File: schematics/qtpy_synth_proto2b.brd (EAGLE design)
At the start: 76.2 x 63.5 mm, 25 parts, among them IC1 H11L1MS, J1 AUDIO-JACK-TRRS, J2 AUDIO-JACK-TRRS, P1 10k, P2 10k, U1 ADAFRUIT_QTPYM0

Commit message: sync up
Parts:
- DISP: value DISPLAY-OLED-128X64-I2C -> DISPLAY-OLED-128X64-I2CTOD; device diy-modules:DISPLAY-OLED-128X64-I2C -> todstuff2023:DISPLAY-OLED-128X64-I2C-TOD
- moved SW 2.54 mm to (38.1, 15.2)
- moved P1 2.54 mm to (14.0, 25.4)
- moved P2 2.54 mm to (62.2, 25.4)
- moved U1 0.76 mm to (14.5, 47.0)
- renumbered C11 to C1
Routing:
- net +3V3: track 154.1 -> 150.7 mm
- net POTA: track 43.9 -> 41.7 mm
- net POTB: track 75.0 -> 73.1 mm
- net TP4: track 75.1 -> 74.3 mm
- net TP2: track 74.5 -> 75.3 mm
- net SDA: track 50.8 -> 50.1 mm
- net PWM_AUDIO: track 40.0 -> 40.8 mm
- net MIDI_IN: track 37.5 -> 38.3 mm
- net SCL: track 47.8 -> 47.0 mm
- net SW: track 67.0 -> 67.7 mm
- net TP3: track 68.5 -> 69.2 mm
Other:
- board text added: "Parts: - QTPy RP2040 - 0.9" I2C OLED SSD1306 - 2x 10k pots - tact switch - 2x PJ320D 3.5mm jacks - IC1: H11L1 optoisolator - D1: 1N4148 - R1-4: 1M, R5: 4.7k, R6,R7: 220, R8:100: R9 1.8k - C1,C2: 100nF, C3: 47uF"
- board text added: "qtpy_synth_proto2b"
- board text removed: "Parts: - QTPy RP2040 - 0.9" I2C OLED SSD1306 - 2x 10k pots - tact switch - IC1: H11L1 optoisolator - D1: 1N4148 - R1-4: 1M, R5: 4.7k, R6,R7: 220, R8:100: R9 1.8k - C1,C2: 100nF, C3: 47uF"
- board text removed: "qtpy_synth_proto2a"

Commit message: more progress on synthio_instrument
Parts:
- moved P1 2.54 mm to (14.0, 22.9)
- moved P2 2.54 mm to (62.2, 22.9)
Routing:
- net SW: track 67.7 -> 70.9 mm
- net POTB: track 73.1 -> 75.8 mm
- net POTA: track 41.7 -> 44.2 mm
- net TP1: track 53.1 -> 55.4 mm
- net TP2: track 75.3 -> 77.1 mm
- net +3V3: track 150.7 -> 151.3 mm

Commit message: gerbers for proto2b
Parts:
- moved R4 2.74 mm to (62.2, 11.4)
- moved R1 0.76 mm to (14.0, 11.4)
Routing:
- net TP4: track 74.3 -> 76.4 mm
- net TP1: track 55.4 -> 56.6 mm
- net TP2: track 77.1 -> 76.1 mm
- net MIDI_IN: track 38.3 -> 37.4 mm
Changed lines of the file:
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@@
 <layer number="14" name="Route14" color="1" fill="6" visible="no" active="no"/>
 <layer number="15" name="Route15" color="4" fill="6" visible="no" active="no"/>
-<layer number="16" name="Bottom" color="1" fill="1" visible="yes" active="yes"/>
+<layer number="16" name="Bottom" color="1" fill="1" visible="no" active="yes"/>
 <layer number="17" name="Pads" color="2" fill="1" visible="yes" active="yes"/>
 <layer number="18" name="Vias" color="2" fill="1" visible="yes" active="yes"/>
@@
 <layer number="20" name="Dimension" color="15" fill="1" visible="yes" active="yes"/>
 <layer number="21" name="tPlace" color="14" fill="1" visible="yes" active="yes"/>
-<layer number="22" name="bPlace" color="13" fill="1" visible="yes" active="yes"/>
+<layer number="22" name="bPlace" color="13" fill="1" visible="no" active="yes"/>
 <layer number="23" name="tOrigins" color="15" fill="1" visible="yes" active="yes"/>
-<layer number="24" name="bOrigins" color="15" fill="1" visible="yes" active="yes"/>
+<layer number="24" name="bOrigins" color="15" fill="1" visible="no" active="yes"/>
 <layer number="25" name="tNames" color="7" fill="1" visible="yes" active="yes"/>
-<layer number="26" name="bNames" color="7" fill="1" visible="yes" active="yes"/>
+<layer number="26" name="bNames" color="7" fill="1" visible="no" active="yes"/>
 <layer number="27" name="tValues" color="7" fill="1" visible="no" active="yes"/>
 <layer number="28" name="bValues" color="7" fill="1" visible="no" active="yes"/>
@@
 <layer number="38" name="bTest" color="7" fill="1" visible="no" active="yes"/>
 <layer number="39" name="tKeepout" color="4" fill="11" visible="yes" active="yes"/>
-<layer number="40" name="bKeepout" color="1" fill="11" visible="yes" active="yes"/>
+<layer number="40" name="bKeepout" color="1" fill="11" visible="no" active="yes"/>
 <layer number="41" name="tRestrict" color="4" fill="10" visible="yes" active="yes"/>
-<layer number="42" name="bRestrict" color="1" fill="10" visible="yes" active="yes"/>
+<layer number="42" name="bRestrict" color="1" fill="10" visible="no" active="yes"/>
 <layer number="43" name="vRestrict" color="2" fill="10" visible="no" active="yes"/>
 <layer number="44" name="Drills" color="7" fill="1" visible="no" active="yes"/>
@@
 <layer number="50" name="dxf" color="7" fill="1" visible="no" active="yes"/>
 <layer number="51" name="tDocu" color="7" fill="1" visible="yes" active="yes"/>
-<layer number="52" name="bDocu" color="7" fill="1" visible="yes" active="yes"/>
+<layer number="52" name="bDocu" color="7" fill="1" visible="no" active="yes"/>
 <layer number="53" name="tGND_GNDA" color="7" fill="9" visible="no" active="no"/>
 <layer number="54" name="bGND_GNDA" color="1" fill="9" visible="no" active="no"/>
@@
 <text x="72.39" y="34.29" size="1.016" layer="22" ratio="10" rot="MR0">works with CircuitPython!</text>
 <wire x1="-2.54" y1="22.86" x2="77.47" y2="22.86" width="0.1524" layer="51" style="shortdash"/>
+<wire x1="-3.81" y1="11.43" x2="76.2" y2="11.43" width="0.1524" layer="51" style="shortdash"/>
 </plain>
 <attributes>
@@
 <attribute name="MPN" value="PJ-320D" x="63.5" y="58.42" size="1.778" layer="27" rot="R270" display="off"/>
 </element>
-<element name="R1" library="rcl" library_urn="urn:adsk.eagle:library:334" package="R0805" package3d_urn="urn:adsk.eagle:package:23553/2" value="1M" x="13.97" y="10.668" smashed="yes">
-<attribute name="NAME" x="13.589" y="11.684" size="1.016" layer="25" ratio="10"/>
-<attribute name="POPULARITY" value="86" x="13.97" y="10.668" size="1.778" layer="27" display="off"/>
-<attribute name="SPICEPREFIX" value="R" x="13.97" y="10.668" size="1.778" layer="27" display="off"/>
-<attribute name="VALUE" x="13.335" y="8.128" size="1.27" layer="27"/>
+<element name="R1" library="rcl" library_urn="urn:adsk.eagle:library:334" package="R0805" package3d_urn="urn:adsk.eagle:package:23553/2" value="1M" x="13.97" y="11.43" smashed="yes">
+<attribute name="NAME" x="13.589" y="12.446" size="1.016" layer="25" ratio="10"/>
+<attribute name="POPULARITY" value="86" x="13.97" y="11.43" size="1.778" layer="27" display="off"/>
+<attribute name="SPICEPREFIX" value="R" x="13.97" y="11.43" size="1.778" layer="27" display="off"/>
+<attribute name="VALUE" x="13.335" y="8.89" size="1.27" layer="27"/>
 </element>
 <element name="R2" library="rcl" library_urn="urn:adsk.eagle:library:334" package="R0805" package3d_urn="urn:adsk.eagle:package:23553/2" value="1M" x="29.21" y="15.24" smashed="yes">
@@
 <attribute name="VALUE" x="46.355" y="12.7" size="1.27" layer="27"/>
 </element>
-<element name="R4" library="rcl" library_urn="urn:adsk.eagle:library:334" package="R0805" package3d_urn="urn:adsk.eagle:package:23553/2" value="1M" x="59.69" y="10.414" smashed="yes">
-<attribute name="NAME" x="59.055" y="11.684" size="1.016" layer="25" ratio="10"/>
-<attribute name="POPULARITY" value="86" x="59.69" y="10.414" size="1.778" layer="27" display="off"/>
-<attribute name="SPICEPREFIX" value="R" x="59.69" y="10.414" size="1.778" layer="27" display="off"/>
-<attribute name="VALUE" x="59.055" y="7.874" size="1.27" layer="27"/>
+<element name="R4" library="rcl" library_urn="urn:adsk.eagle:library:334" package="R0805" package3d_urn="urn:adsk.eagle:package:23553/2" value="1M" x="62.23" y="11.43" smashed="yes">
+<attribute name="NAME" x="61.595" y="12.7" size="1.016" layer="25" ratio="10"/>
+<attribute name="POPULARITY" value="86" x="62.23" y="11.43" size="1.778" layer="27" display="off"/>
+<attribute name="SPICEPREFIX" value="R" x="62.23" y="11.43" size="1.778" layer="27" display="off"/>
+<attribute name="VALUE" x="61.595" y="8.89" size="1.27" layer="27"/>
 </element>
 <element name="DISP" library="todstuff2023" package="DISPLAY-OLED-128X64-I2C-TOD" value="DISPLAY-OLED-128X64-I2CTOD" x="38.1" y="35.56" smashed="yes" rot="R180">
@@
 <wire x1="45.974" y1="29.21" x2="44.45" y2="29.21" width="0.3048" layer="1"/>
 <wire x1="41.221" y1="29.21" x2="36.395" y2="34.036" width="0.254" layer="1"/>
-<wire x1="51.635" y1="33.02" x2="46.99" y2="33.02" width="0.254" layer="1"/>
-<wire x1="46.99" y1="33.02" x2="45.974" y2="32.004" width="0.254" layer="1"/>
-<wire x1="45.974" y1="32.004" x2="45.974" y2="29.21" width="0.254" layer="1"/>
+<wire x1="51.635" y1="33.02" x2="48.514" y2="33.02" width="0.254" layer="1"/>
+<wire x1="48.514" y1="33.02" x2="45.974" y2="30.48" width="0.254" layer="1"/>
+<wire x1="45.974" y1="30.48" x2="45.974" y2="29.21" width="0.254" layer="1"/>
 <wire x1="45.974" y1="29.21" x2="45.974" y2="27.94" width="0.254" layer="1"/>
 <wire x1="44.45" y1="29.21" x2="41.221" y2="29.21" width="0.254" layer="1"/>
@@
 <contactref element="U1" pad="A3"/>
 <wire x1="11.43" y1="2.54" x2="13.02" y2="4.13" width="0.3048" layer="1"/>
-<wire x1="13.02" y1="4.13" x2="13.02" y2="10.668" width="0.3048" layer="1"/>
+<wire x1="13.02" y1="4.13" x2="13.02" y2="11.43" width="0.3048" layer="1"/>
 <wire x1="9.398" y1="45.212" x2="9.398" y2="35.56" width="0.3048" layer="1"/>
-<wire x1="9.398" y1="35.56" x2="4.826" y2="30.988" width="0.3048" layer="1"/>
-<wire x1="4.826" y1="30.988" x2="4.826" y2="12.954" width="0.3048" layer="1"/>
-<wire x1="4.826" y1="12.954" x2="7.112" y2="10.668" width="0.3048" layer="1"/>
-<wire x1="7.112" y1="10.668" x2="13.02" y2="10.668" width="0.3048" layer="1"/>
+<wire x1="9.398" y1="35.56" x2="3.81" y2="29.972" width="0.3048" layer="1"/>
+<wire x1="3.81" y1="29.972" x2="3.81" y2="13.97" width="0.3048" layer="1"/>
+<wire x1="3.81" y1="13.97" x2="6.35" y2="11.43" width="0.3048" layer="1"/>
+<wire x1="6.35" y1="11.43" x2="13.02" y2="11.43" width="0.3048" layer="1"/>
 </signal>
 <signal name="TP2">
@@
 <wire x1="6.858" y1="49.53" x2="7.874" y2="49.53" width="0.3048" layer="1"/>
 <wire x1="11.176" y1="46.228" x2="11.176" y2="34.798" width="0.3048" layer="1"/>
-<wire x1="6.3364" y1="29.9584" x2="6.3364" y2="13.9836" width="0.3048" layer="1"/>
-<wire x1="8.2924" y1="12.0276" x2="25.0476" y2="12.0276" width="0.3048" layer="1"/>
-<wire x1="11.176" y1="34.798" x2="6.3364" y2="29.9584" width="0.3048" layer="1"/>
-<wire x1="6.3364" y1="13.9836" x2="8.2924" y2="12.0276" width="0.3048" layer="1"/>
+<wire x1="5.5744" y1="29.1964" x2="5.5744" y2="15.7616" width="0.3048" layer="1"/>
+<wire x1="8.0384" y1="13.2976" x2="24.7936" y2="13.2976" width="0.3048" layer="1"/>
+<wire x1="11.176" y1="34.798" x2="5.5744" y2="29.1964" width="0.3048" layer="1"/>
+<wire x1="5.5744" y1="15.7616" x2="8.0384" y2="13.2976" width="0.3048" layer="1"/>
 <wire x1="29.21" y1="2.54" x2="29.21" y2="12.954" width="0.3048" layer="1"/>
 <wire x1="29.21" y1="12.954" x2="28.26" y2="13.904" width="0.3048" layer="1"/>
 <wire x1="28.26" y1="13.904" x2="28.26" y2="15.24" width="0.3048" layer="1"/>
-<wire x1="25.0476" y1="12.0276" x2="28.26" y2="15.24" width="0.3048" layer="1"/>
+<wire x1="26.736" y1="15.24" x2="24.7936" y2="13.2976" width="0.3048" layer="1"/>
+<wire x1="26.736" y1="15.24" x2="28.26" y2="15.24" width="0.3048" layer="1"/>
 </signal>
 <signal name="TP3">
@@
 <contactref element="R4" pad="1"/>
 <wire x1="18.542" y1="40.64" x2="19.812" y2="41.91" width="0.3048" layer="1"/>
-<wire x1="64.77" y1="2.54" x2="58.74" y2="8.57" width="0.3048" layer="1"/>
-<wire x1="58.74" y1="8.57" x2="58.74" y2="10.414" width="0.3048" layer="1"/>
-<wire x1="58.74" y1="10.414" x2="56.896" y2="10.414" width="0.3048" layer="1"/>
-<wire x1="56.896" y1="10.414" x2="46.736" y2="20.574" width="0.3048" layer="1"/>
+<wire x1="64.77" y1="2.54" x2="61.28" y2="6.03" width="0.3048" layer="1"/>
+<wire x1="61.28" y1="6.03" x2="61.28" y2="11.43" width="0.3048" layer="1"/>
+<wire x1="61.28" y1="11.43" x2="55.88" y2="11.43" width="0.3048" layer="1"/>
+<wire x1="55.88" y1="11.43" x2="46.736" y2="20.574" width="0.3048" layer="1"/>
 <contactref element="U1" pad="SCK"/>
 <wire x1="19.812" y1="41.91" x2="22.098" y2="41.91" width="0.3048" layer="1"/>

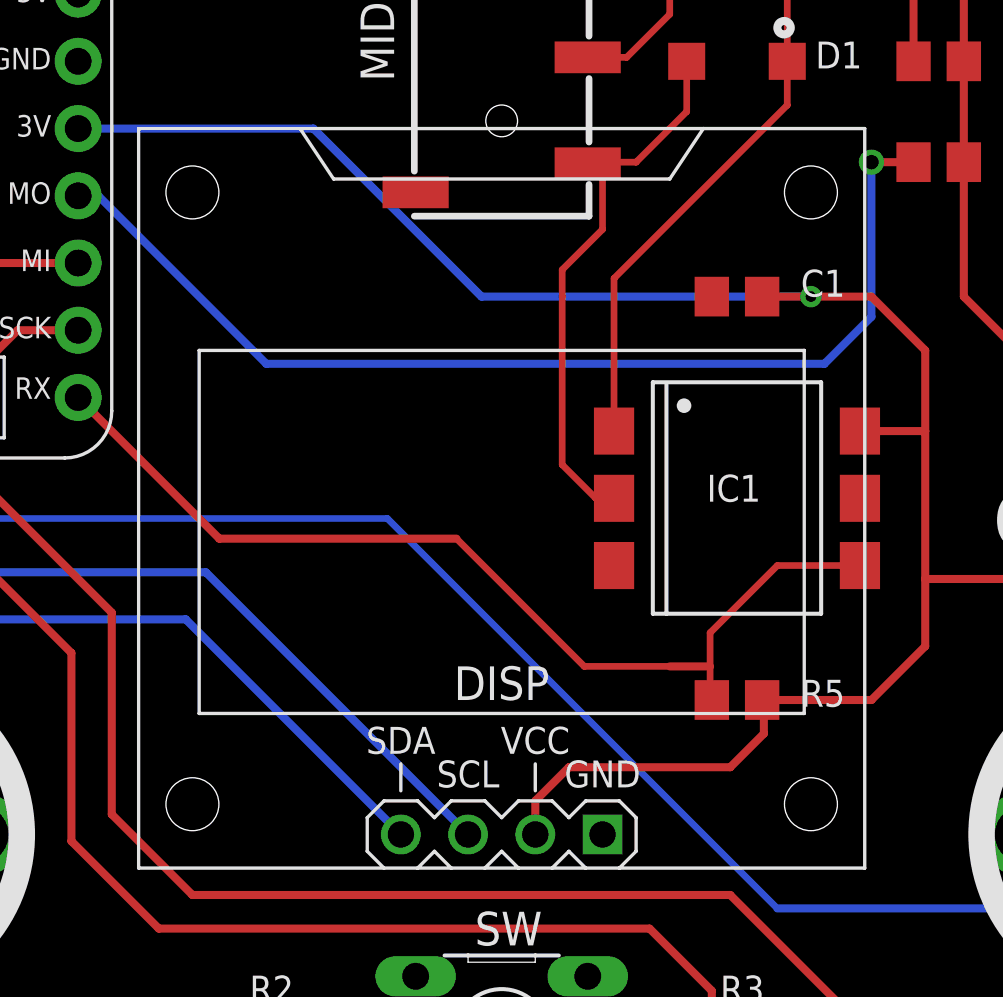
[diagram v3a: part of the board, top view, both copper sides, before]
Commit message: fix oled holes
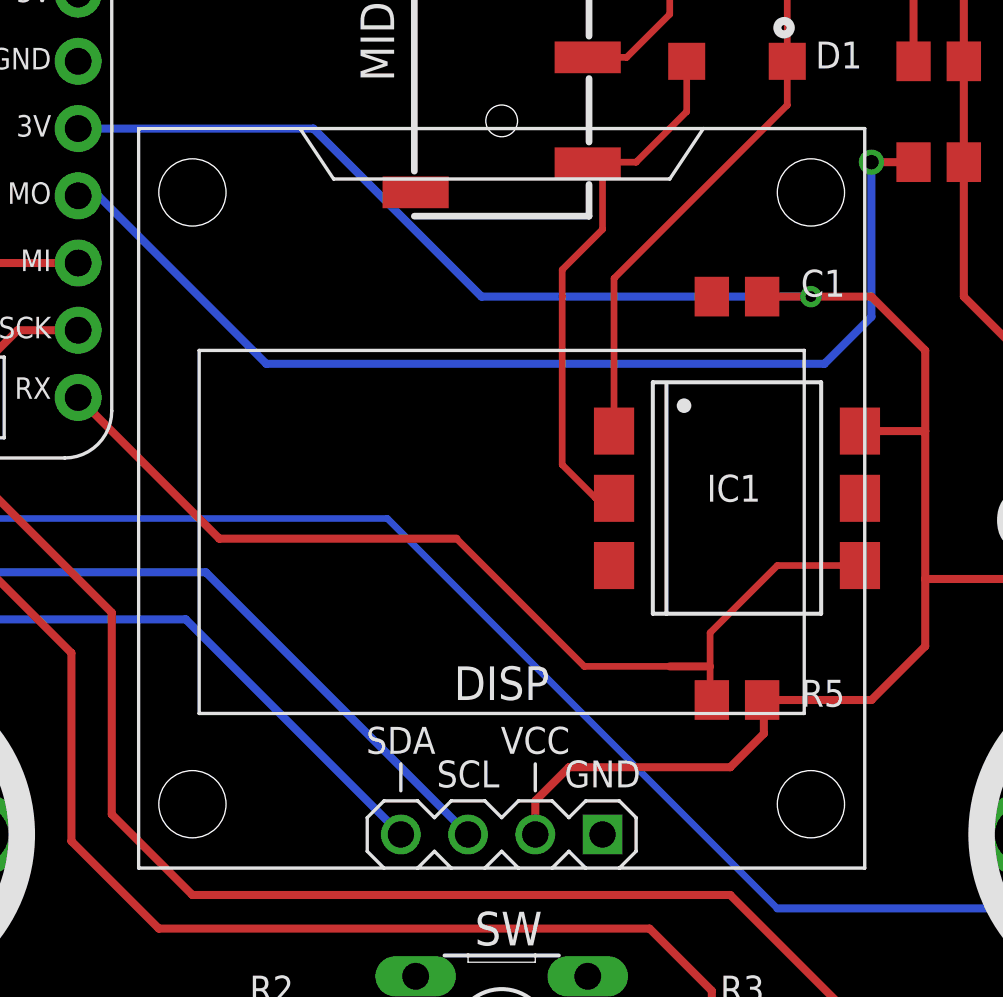
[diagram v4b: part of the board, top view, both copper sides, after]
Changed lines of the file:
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@@
 <layer number="14" name="Route14" color="1" fill="6" visible="no" active="no"/>
 <layer number="15" name="Route15" color="4" fill="6" visible="no" active="no"/>
-<layer number="16" name="Bottom" color="1" fill="1" visible="no" active="yes"/>
+<layer number="16" name="Bottom" color="1" fill="1" visible="yes" active="yes"/>
 <layer number="17" name="Pads" color="2" fill="1" visible="yes" active="yes"/>
 <layer number="18" name="Vias" color="2" fill="1" visible="yes" active="yes"/>
@@
 <layer number="20" name="Dimension" color="15" fill="1" visible="yes" active="yes"/>
 <layer number="21" name="tPlace" color="14" fill="1" visible="yes" active="yes"/>
-<layer number="22" name="bPlace" color="13" fill="1" visible="no" active="yes"/>
+<layer number="22" name="bPlace" color="13" fill="1" visible="yes" active="yes"/>
 <layer number="23" name="tOrigins" color="15" fill="1" visible="yes" active="yes"/>
-<layer number="24" name="bOrigins" color="15" fill="1" visible="no" active="yes"/>
+<layer number="24" name="bOrigins" color="15" fill="1" visible="yes" active="yes"/>
 <layer number="25" name="tNames" color="7" fill="1" visible="yes" active="yes"/>
-<layer number="26" name="bNames" color="7" fill="1" visible="no" active="yes"/>
+<layer number="26" name="bNames" color="7" fill="1" visible="yes" active="yes"/>
 <layer number="27" name="tValues" color="7" fill="1" visible="no" active="yes"/>
 <layer number="28" name="bValues" color="7" fill="1" visible="no" active="yes"/>
@@
 <layer number="38" name="bTest" color="7" fill="1" visible="no" active="yes"/>
 <layer number="39" name="tKeepout" color="4" fill="11" visible="yes" active="yes"/>
-<layer number="40" name="bKeepout" color="1" fill="11" visible="no" active="yes"/>
+<layer number="40" name="bKeepout" color="1" fill="11" visible="yes" active="yes"/>
 <layer number="41" name="tRestrict" color="4" fill="10" visible="yes" active="yes"/>
-<layer number="42" name="bRestrict" color="1" fill="10" visible="no" active="yes"/>
+<layer number="42" name="bRestrict" color="1" fill="10" visible="yes" active="yes"/>
 <layer number="43" name="vRestrict" color="2" fill="10" visible="no" active="yes"/>
 <layer number="44" name="Drills" color="7" fill="1" visible="no" active="yes"/>
-<layer number="45" name="Holes" color="7" fill="1" visible="no" active="yes"/>
+<layer number="45" name="Holes" color="7" fill="1" visible="yes" active="yes"/>
 <layer number="46" name="Milling" color="3" fill="1" visible="no" active="yes"/>
-<layer number="47" name="Measures" color="7" fill="1" visible="no" active="yes"/>
-<layer number="48" name="Document" color="7" fill="1" visible="no" active="yes"/>
-<layer number="49" name="Reference" color="7" fill="1" visible="no" active="yes"/>
+<layer number="47" name="Measures" color="7" fill="1" visible="yes" active="yes"/>
+<layer number="48" name="Document" color="7" fill="1" visible="yes" active="yes"/>
+<layer number="49" name="Reference" color="7" fill="1" visible="yes" active="yes"/>
 <layer number="50" name="dxf" color="7" fill="1" visible="no" active="yes"/>
 <layer number="51" name="tDocu" color="7" fill="1" visible="yes" active="yes"/>
-<layer number="52" name="bDocu" color="7" fill="1" visible="no" active="yes"/>
+<layer number="52" name="bDocu" color="7" fill="1" visible="yes" active="yes"/>
 <layer number="53" name="tGND_GNDA" color="7" fill="9" visible="no" active="no"/>
 <layer number="54" name="bGND_GNDA" color="1" fill="9" visible="no" active="no"/>
@@
 <layer number="114" name="tPlaceRed" color="7" fill="1" visible="no" active="yes"/>
 <layer number="115" name="FRNTMAAT2" color="7" fill="1" visible="no" active="yes"/>
-<layer number="116" name="Patch_BOT" color="9" fill="4" visible="no" active="yes"/>
+<layer number="116" name="Patch_BOT" color="9" fill="4" visible="yes" active="yes"/>
 <layer number="117" name="BACKMAAT1" color="7" fill="1" visible="no" active="yes"/>
 <layer number="118" name="Rect_Pads" color="7" fill="1" visible="no" active="no"/>
@@
 <layer number="196" name="mValues" color="7" fill="1" visible="no" active="yes"/>
 <layer number="199" name="Contour" color="7" fill="1" visible="no" active="yes"/>
-<layer number="200" name="200bmp" color="14" fill="10" visible="no" active="yes"/>
-<layer number="201" name="201bmp" color="13" fill="1" visible="no" active="yes"/>
-<layer number="202" name="202bmp" color="3" fill="1" visible="no" active="yes"/>
+<layer number="200" name="200bmp" color="14" fill="10" visible="yes" active="yes"/>
+<layer number="201" name="201bmp" color="13" fill="1" visible="yes" active="yes"/>
+<layer number="202" name="202bmp" color="3" fill="1" visible="yes" active="yes"/>
 <layer number="203" name="203bmp" color="4" fill="10" visible="no" active="yes"/>
 <layer number="204" name="204bmp" color="5" fill="10" visible="no" active="yes"/>
@@
 <layer number="206" name="206bmp" color="7" fill="10" visible="no" active="yes"/>
 <layer number="207" name="207bmp" color="8" fill="10" visible="no" active="yes"/>
-<layer number="208" name="208bmp" color="9" fill="10" visible="no" active="yes"/>
-<layer number="209" name="209bmp" color="7" fill="1" visible="no" active="yes"/>
+<layer number="208" name="208bmp" color="9" fill="10" visible="yes" active="yes"/>
+<layer number="209" name="209bmp" color="7" fill="1" visible="yes" active="yes"/>
 <layer number="210" name="210bmp" color="7" fill="1" visible="no" active="yes"/>
 <layer number="211" name="211bmp" color="7" fill="1" visible="no" active="yes"/>
@@
 </layers>
 <board>
-<fusionsync huburn="a.cGVyc29uYWw6dWUyOWMzMmM3" projecturn="a.cGVyc29uYWw6dWUyOWMzMmM3IzIwMTgwMjExMTE3NDU0Nzgx" f3durn="urn:adsk.wipprod:dm.lineage:n3cez0FGSMK2FoViouMuSg" pcbguid="950806e0-2892-439c-99f6-5b3d1844623e" lastpulledtime="" lastsyncedchangeguid="" latestrevisionid="7b3c2d8b-8aa2-45a8-9544-a03aa6eb5537" lastsyncedrevisionid="7b3c2d8b-8aa2-45a8-9544-a03aa6eb5537" lastboardhashguid="4e715841-c75d-99ce-1d71-2c272b38c34e" lastpushedtime="2023-07-14T18:15:02Z" linktopcb3d="true"/>
+<fusionsync huburn="a.cGVyc29uYWw6dWUyOWMzMmM3" projecturn="a.cGVyc29uYWw6dWUyOWMzMmM3IzIwMTgwMjExMTE3NDU0Nzgx" f3durn="urn:adsk.wipprod:dm.lineage:n3cez0FGSMK2FoViouMuSg" pcbguid="" lastpulledtime="" lastsyncedchangeguid="" latestrevisionid="7b3c2d8b-8aa2-45a8-9544-a03aa6eb5537" lastsyncedrevisionid="7b3c2d8b-8aa2-45a8-9544-a03aa6eb5537" lastboardhashguid="4e715841-c75d-99ce-1d71-2c272b38c34e" lastpushedtime="2023-07-14T18:15:02Z" linktopcb3d="true"/>
 <plain>
 <wire x1="0" y1="-2.54" x2="0" y2="55.88" width="0" layer="20"/>
